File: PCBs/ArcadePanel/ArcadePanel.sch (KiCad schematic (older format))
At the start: 48 parts, among them J1 Screw_Terminal_01x10, J10 1, J11 1, J12 1, J13 1, J14 1, J15 1, J16 1, J17 1, J18 1, J19 1, J2 Screw_Terminal_01x10, J20 1, J21 1, J22 1, J23 1, J24 1, J25 1, J26 1, J27 1, J28 1, J29 1, J3 Screw_Terminal_01x12, J30 1, J31 1, J32 1, J33 1, J34 1, J35 1, J36 1, J37 1, J38 1, J39 1, J4 Screw_Terminal_01x12, J40 1, J41 1, J42 1, J43 1, J44 1, J45 1, J46 1, J47 1, J48 1, J5 A1, J6 A2, J7 A3, J8 1, J9 1

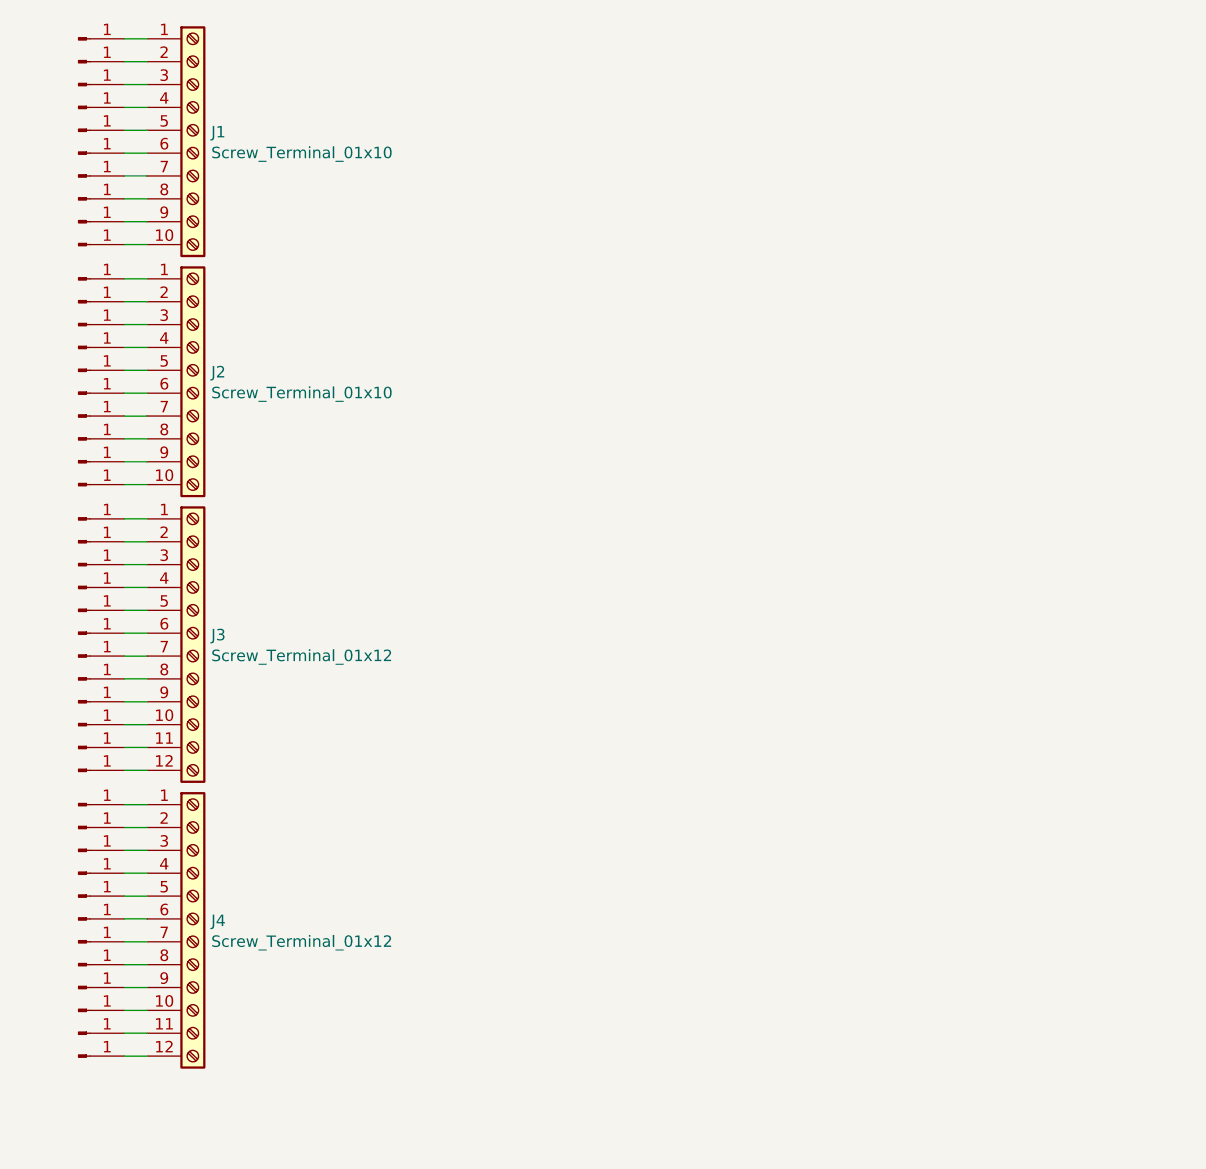
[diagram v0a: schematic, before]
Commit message: v2 PCB revisions: switch to ribbon cable rather than PCB edge, add DIP switch for panel identifications
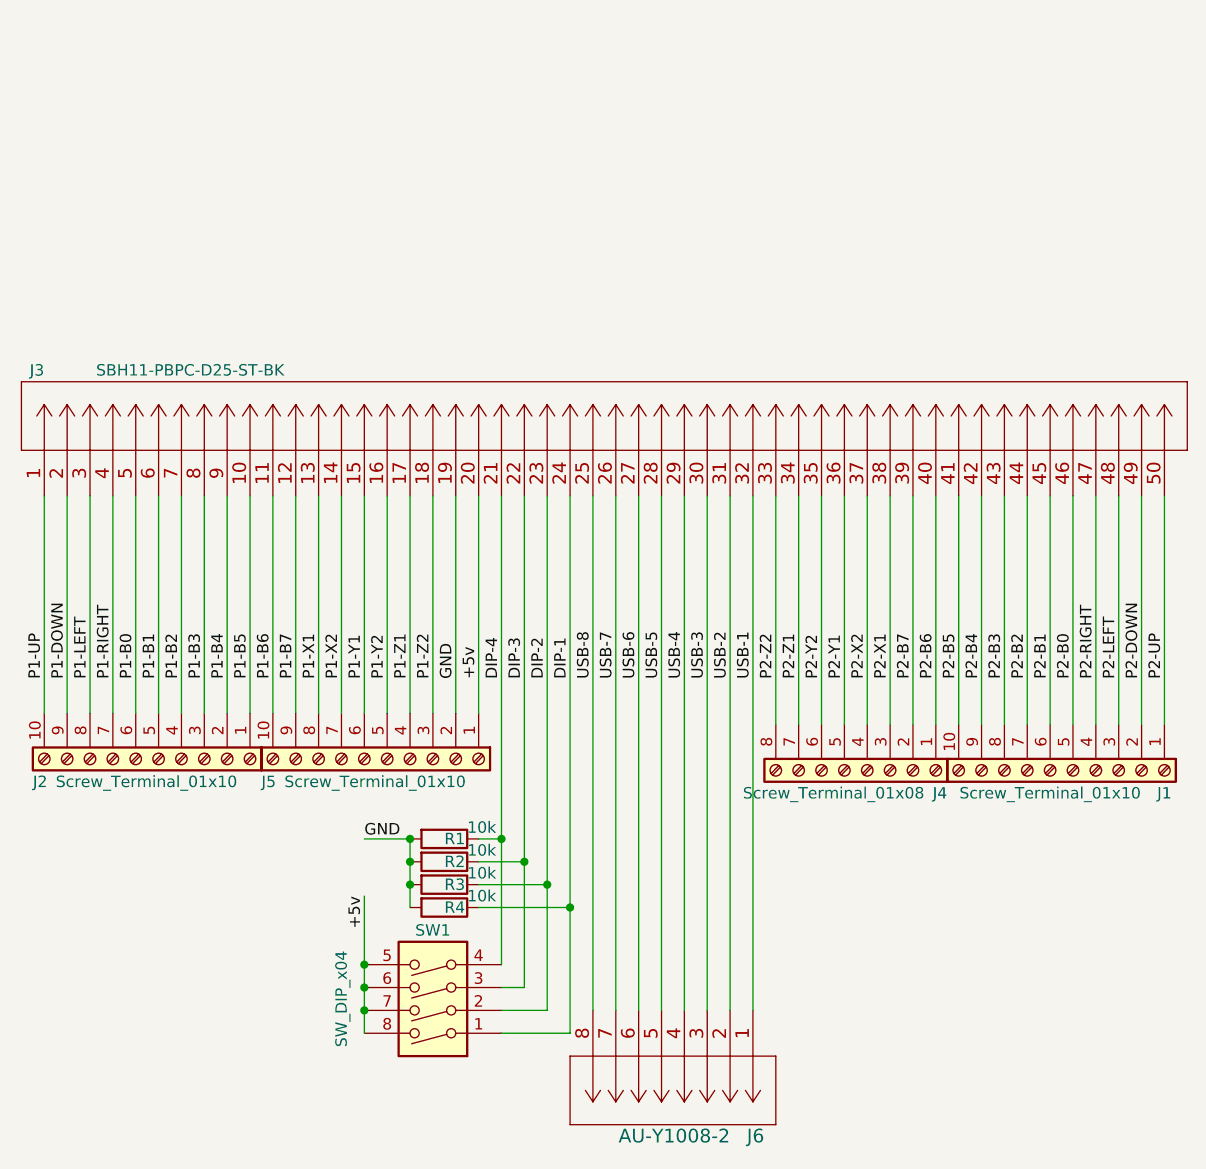
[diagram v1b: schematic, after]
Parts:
- removed J10, J11, J12, J13, J14, J15, J16, J17, J18, J19, J20, J21, J22, J23, J24, J25, J26, J27, J28, J29, J30, J31, J32, J33, J34, J35, J36, J37, J38, J39, J40, J41, J42, J43, J44, J45, J46, J47, J48, J8, J9: 1, TestPoint:TestPoint_Pad_1.0x1.0mm-nosilk, symbol Connector:Conn_01x01_Male
- removed J3, J4: Screw_Terminal_01x12, TB001-500-12BE:CUI_TB001-500-12BE, symbol Connector:Screw_Terminal_01x12
- removed J5: A1, TestPoint:TestPoint_Pad_1.0x1.0mm-nosilk, symbol Connector:Conn_01x01_Male
- removed J6: A2, TestPoint:TestPoint_Pad_1.0x1.0mm-nosilk, symbol Connector:Conn_01x01_Male
- removed J7: A3, TestPoint:TestPoint_Pad_1.0x1.0mm-nosilk, symbol Connector:Conn_01x01_Male
- added J3: SBH11-PBPC-D25-ST-BK, ul_SBH11PBPCD25STBK:SBH11-PBPC-D25-ST-BK, symbol 2020-07-14_18-22-10:SBH11-PBPC-D25-ST-BK
- added J4: Screw_Terminal_01x08, TB001-500-08BE:CUI_TB001-500-08BE, symbol Connector:Screw_Terminal_01x08
- added J5: Screw_Terminal_01x10, TB001-500-10BE:CUI_TB001-500-10BE, symbol Connector:Screw_Terminal_01x10
- added J6: AU-Y1008-2, AU-Y1008-2:AU-Y1008-2, symbol AU-Y1008-2:AU-Y1008-2
- added R1, R2, R3, R4: 10k, Resistor_THT:R_Axial_DIN0204_L3.6mm_D1.6mm_P7.62mm_Horizontal, symbol Device:R
- added SW1: SW_DIP_x04, digikey-footprints:DIP-8_W7.62mm, symbol Switch:SW_DIP_x04
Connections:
- net P2-UP: now reaches J1.1 (Pin_1)
- net P2-UP: now also J3.50
- net P2-B5: now reaches J1.10 (Pin_10)
- net P2-B5: now also J3.41
- net P2-DOWN: now reaches J1.2 (Pin_2)
- net P2-DOWN: now also J3.49
- net P2-LEFT: now reaches J1.3 (Pin_3)
- net P2-LEFT: now also J3.48
- net P2-RIGHT: now reaches J1.4 (Pin_4)
- net P2-RIGHT: now also J3.47
- net P2-B0: now reaches J1.5 (Pin_5)
- net P2-B0: now also J3.46
- net P2-B1: now reaches J1.6 (Pin_6)
- net P2-B1: now also J3.45
- net P2-B2: now reaches J1.7 (Pin_7)
- net P2-B2: now also J3.44
- net P2-B3: now reaches J1.8 (Pin_8)
- net P2-B3: now also J3.43
- net P2-B4: now reaches J1.9 (Pin_9)
- net P2-B4: now also J3.42
- net P1-B5: now reaches J2.1 (Pin_1)
- net P1-B5: now also J3.10
- net P1-UP: now reaches J2.10 (Pin_10)
- net P1-UP: now also J3.1
- net P1-B4: now reaches J2.2 (Pin_2)
- net P1-B4: now also J3.9
- net P1-B3: now reaches J2.3 (Pin_3)
- net P1-B3: now also J3.8
- net P1-B2: now reaches J2.4 (Pin_4)
- net P1-B2: now also J3.7
- net P1-B1: now reaches J2.5 (Pin_5)
- net P1-B1: now also J3.6
- net P1-B0: now reaches J2.6 (Pin_6)
- net P1-B0: now also J3.5
- net P1-RIGHT: now reaches J2.7 (Pin_7)
- net P1-RIGHT: now also J3.4
- net P1-LEFT: now reaches J2.8 (Pin_8)
- net P1-LEFT: now also J3.3
- net P1-DOWN: now reaches J2.9 (Pin_9)
- net P1-DOWN: now also J3.2
- new net +5v: J3.20, J5.1 (Pin_1), SW1.5, SW1.6, SW1.7, SW1.8
- new net DIP-1: J3.24, R4.1, SW1.1
- new net DIP-2: J3.23, R3.1, SW1.2
- new net DIP-3: J3.22, R2.1, SW1.3
- new net DIP-4: J3.21, R1.1, SW1.4
- new net GND: J3.19, J5.2 (Pin_2), R1.2, R2.2, R3.2, R4.2
- new net P1-B6: J3.11, J5.10 (Pin_10)
- new net P1-B7: J3.12, J5.9 (Pin_9)
- new net P1-X1: J3.13, J5.8 (Pin_8)
- new net P1-X2: J3.14, J5.7 (Pin_7)
- new net P1-Y1: J3.15, J5.6 (Pin_6)
- new net P1-Y2: J3.16, J5.5 (Pin_5)
- new net P1-Z1: J3.17, J5.4 (Pin_4)
- new net P1-Z2: J3.18, J5.3 (Pin_3)
- new net P2-B6: J3.40, J4.1 (Pin_1)
- new net P2-B7: J3.39, J4.2 (Pin_2)
- new net P2-X1: J3.38, J4.3 (Pin_3)
- new net P2-X2: J3.37, J4.4 (Pin_4)
- new net P2-Y1: J3.36, J4.5 (Pin_5)
- new net P2-Y2: J3.35, J4.6 (Pin_6)
- new net P2-Z1: J3.34, J4.7 (Pin_7)
- new net P2-Z2: J3.33, J4.8 (Pin_8)
- new net USB-1: J3.32, J6.1
- new net USB-2: J3.31, J6.2
- new net USB-3: J3.30, J6.3
- new net USB-4: J3.29, J6.4
- new net USB-5: J3.28, J6.5
- new net USB-6: J3.27, J6.6
- new net USB-7: J3.26, J6.7
- new net USB-8: J3.25, J6.8
